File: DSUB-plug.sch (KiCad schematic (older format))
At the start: 1 part, among them J1 DB37_Female

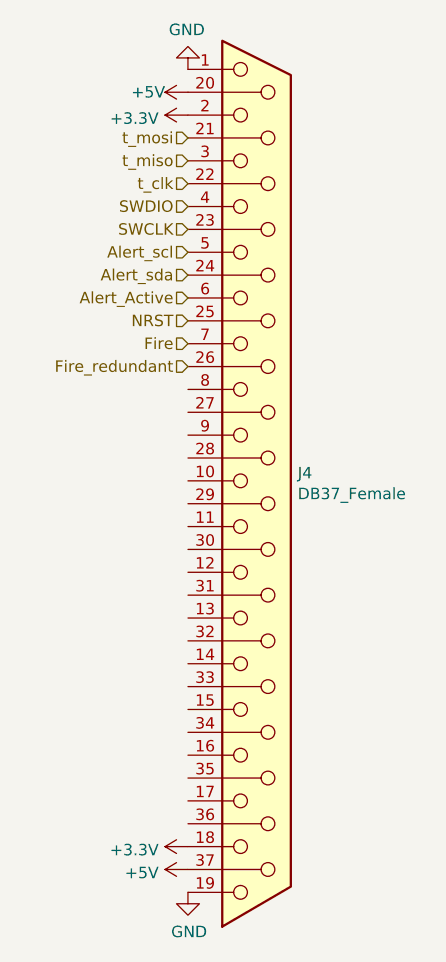
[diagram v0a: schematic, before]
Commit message: Changed layout
Layout was changed. Now we have planes for ground, 5v, and 3v3. hopefully current wont be an issue
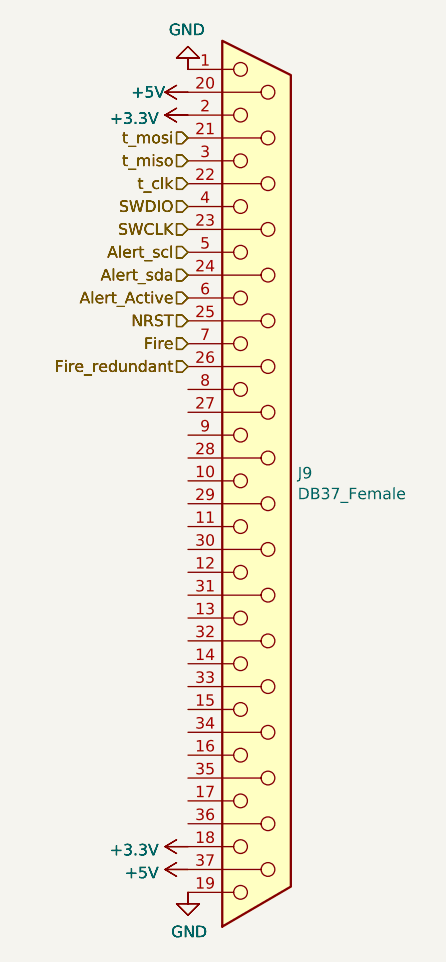
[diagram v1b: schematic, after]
